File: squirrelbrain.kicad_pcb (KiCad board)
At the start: 2 copper layers, 26.1 x 27.8 mm, 21 parts, among them J1 Conn_01x01, J2 Conn_01x01, J3 Conn_01x03, J4 Conn_01x02, J5 Conn_01x02, Q1 SISS80DN-T1-GE3, U1 SEEEDUINO-XIAO-ESP32S3, U2 THVD1420DRLR, U3 THVD1420DRLR, U5 RPM5.0-6.0, U6 SN74LVC2G125DCUR

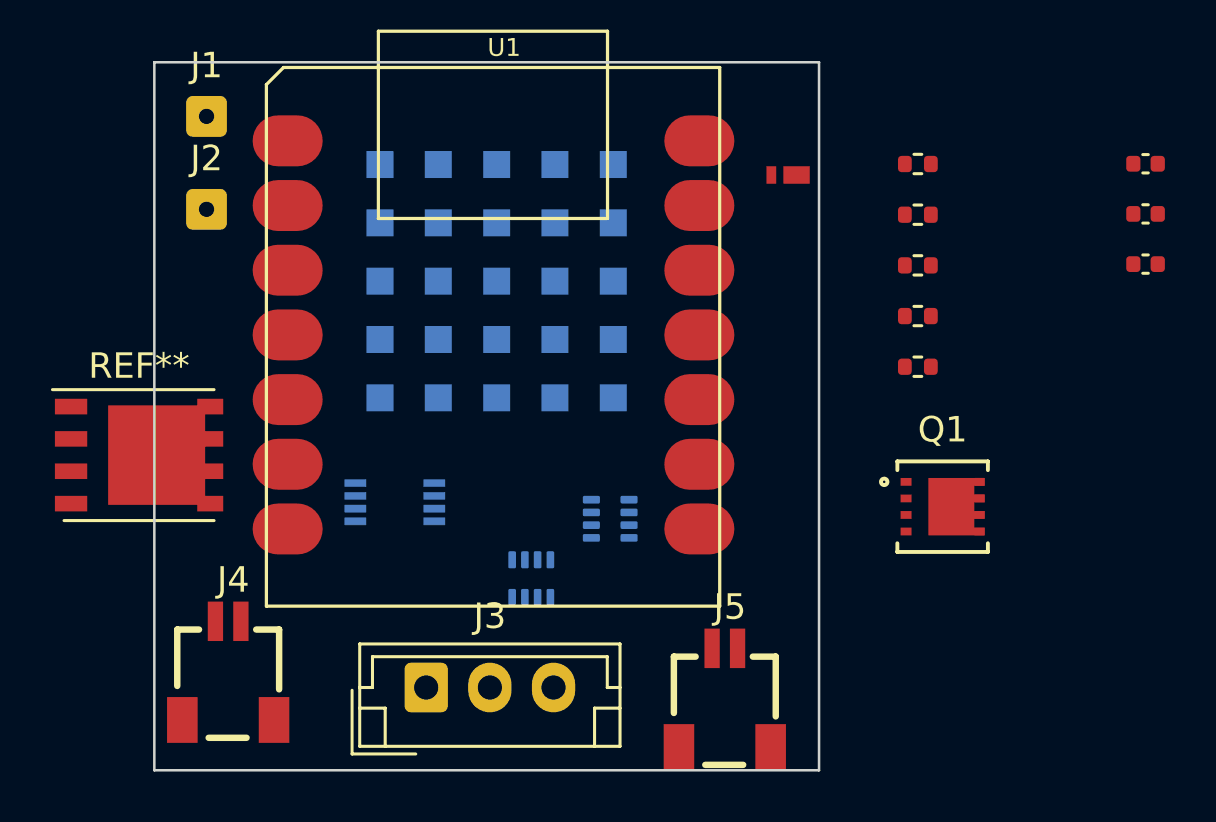
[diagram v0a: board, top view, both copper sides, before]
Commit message: chose high side load switches
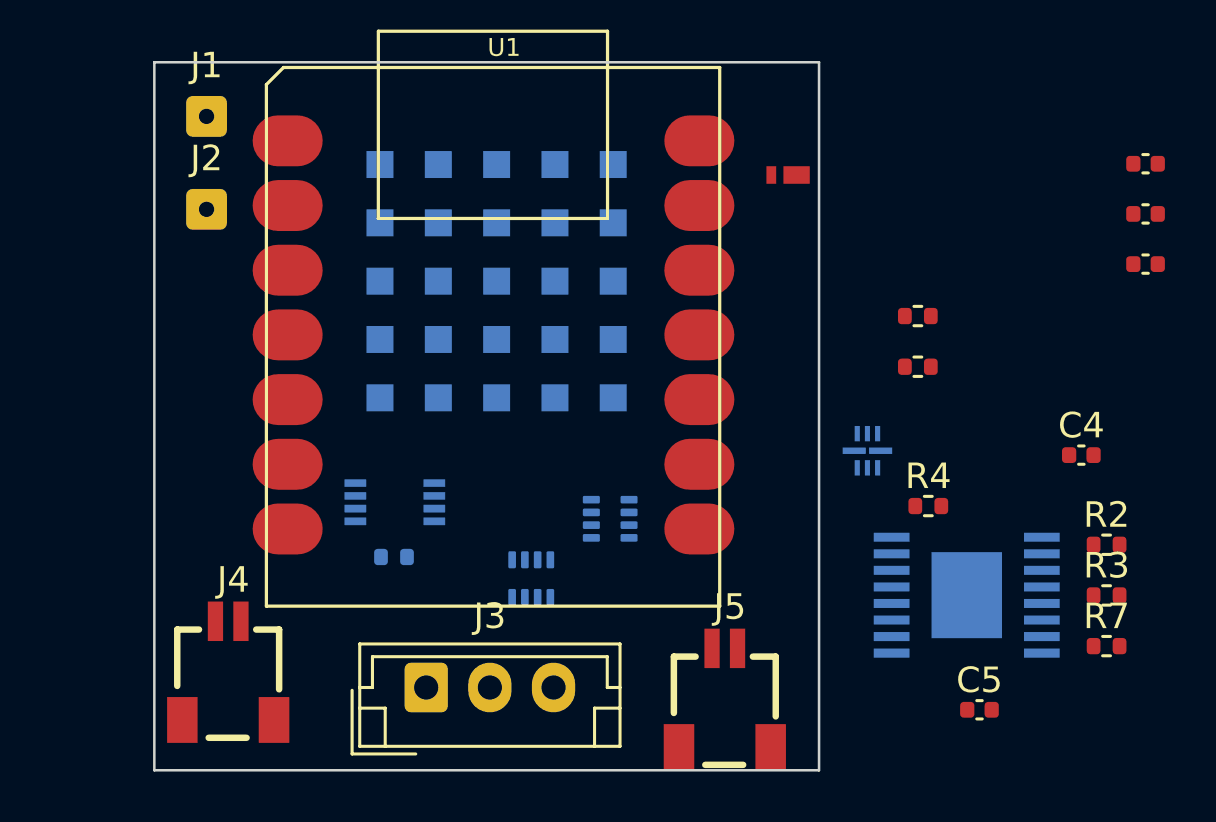
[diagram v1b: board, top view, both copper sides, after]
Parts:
- removed Q1: SISS80DN-T1-GE3, squirrelbrain:SISS80DN
- removed REF**: PowerPAK_SO-8_Single, Package_SO:PowerPAK_SO-8_Single
- added C4: 100nF, Capacitor_SMD:C_0402_1005Metric, F.Cu at (179.5, 98.0)
- added C5: 100nF, Capacitor_SMD:C_0402_1005Metric, F.Cu at (175.5, 108.0)
- added R4: 1k, Resistor_SMD:R_0402_1005Metric, F.Cu at (173.5, 100.0)
- added R7: 10k, Resistor_SMD:R_0402_1005Metric, F.Cu at (180.5, 105.5)
- added U7: TPS1HB08AQPWPRQ1, squirrelbrain:TPS1HB08, B.Cu at (175.0, 103.5)
- added U8: TPS22992SRXNR, squirrelbrain:TPS22992S, B.Cu at (171.1, 97.8)
- R1: moved to B.Cu
- R2: value 54.9k -> 10k
- R3: value 13.7k -> 10k
- moved R1 25.7 mm to (152.5, 102.0), turned to 180 degrees
- moved R3 14.9 mm to (180.5, 103.5)
- moved R2 14.9 mm to (180.5, 101.5)
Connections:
- J3 pad 2: VBUS -> +5VP
- R2 pad 1: /BUS_SENSE -> GND
- R2 pad 2: VBUS -> /MOTOR_ON
- R3 pad 2: /BUS_SENSE -> Net-(U7-SEL1)
- U1 pad 1: unconnected-(U1-PA02_A0_D0-Pad1) -> /MOTOR_ON
- U1 pad 2: /BUS_SENSE -> /GPIO1

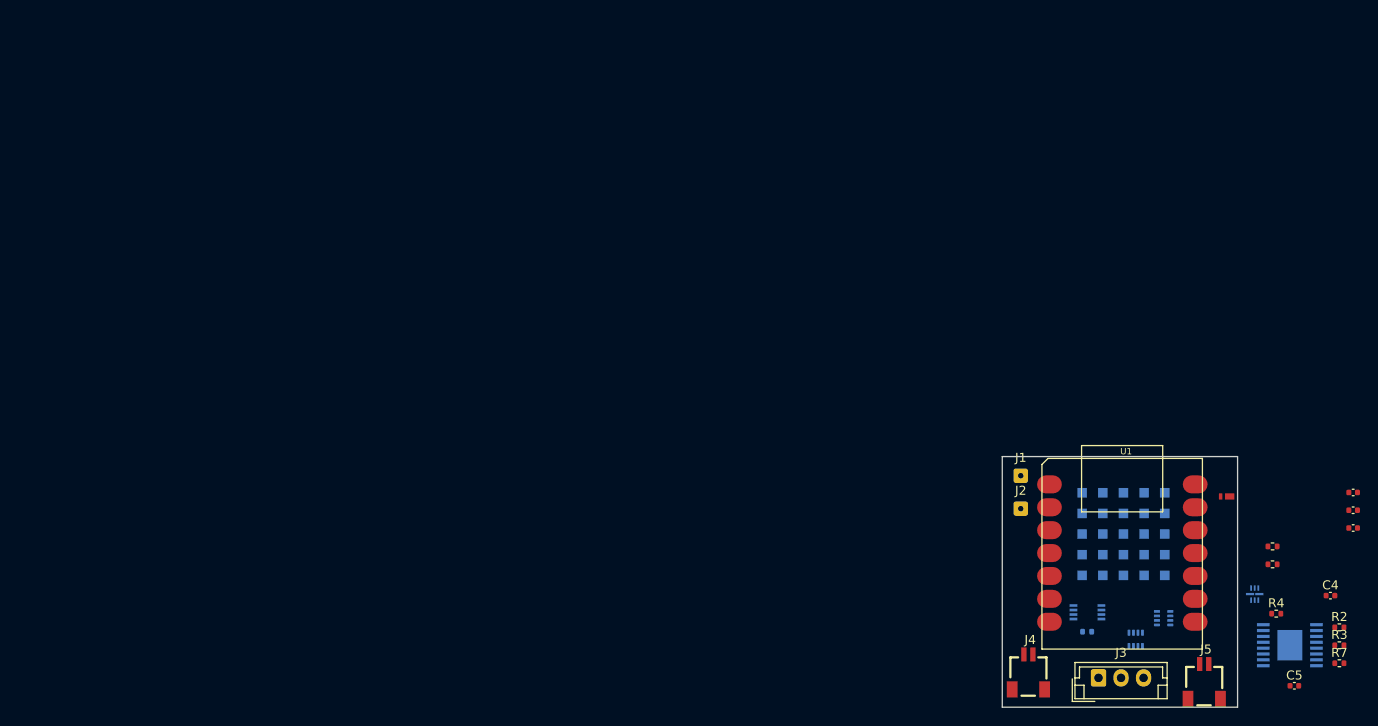
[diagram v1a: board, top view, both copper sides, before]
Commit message: add xt30, start routing
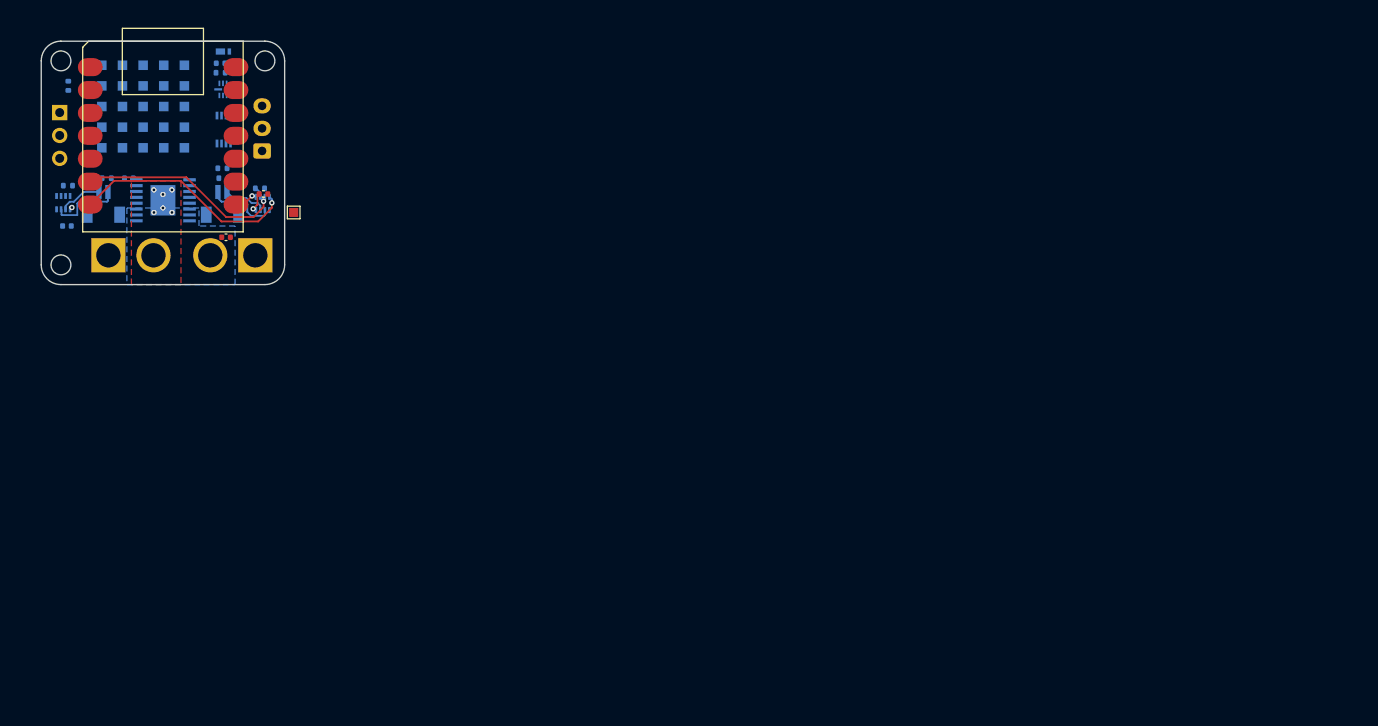
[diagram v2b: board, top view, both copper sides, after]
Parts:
- removed the J2 at (145.2, 88.3)
- added J3: BM02B-SRSS-TB_LF__SN_, squirrelbrain:JST_BM02B-SRSS-TB_LF__SN_, B.Cu at (43.4, 55.8)
- added J6: GPIO1, Connector_PinSocket_2.54mm:PinSocket_1x03_P2.54mm_Vertical, B.Cu at (38.5, 44.4)
- added TP1: SNS, TestPoint:TestPoint_Pad_1.0x1.0mm, F.Cu at (64.5, 55.5)
- C1: renamed from C4; moved to B.Cu
- C3: renamed from C1; moved to B.Cu
- C5: renamed from C2; moved to B.Cu
- D1, R5: moved to B.Cu
- J1: value Conn_01x01 -> BM02B-SRSS-TB_LF__SN_; footprint Connector_Wire:SolderWire-0.1sqmm_1x01_D0.4mm_OD1mm -> squirrelbrain:JST_BM02B-SRSS-TB_LF__SN_; moved to B.Cu
- J2: renamed from J3; moved to B.Cu
- J4: value Conn_01x02 -> BATT; footprint squirrelbrain:JST_SM02B-SRSS-TB(LF)(SN) -> squirrelbrain:AMASS_XT30U-M_1x02_P5.0mm_Vertical; moved to B.Cu
- J5: value Conn_01x02 -> BLDC_PWR; footprint squirrelbrain:JST_SM02B-SRSS-TB(LF)(SN) -> squirrelbrain:AMASS_XT30U-F_1x02_P5.0mm_Vertical; moved to B.Cu
- R1: renamed from R4; moved to B.Cu
- R2: renamed from R3; moved to B.Cu
- R3: renamed from R7; moved to B.Cu
- R4: renamed from R2; moved to B.Cu
- R7: renamed from R6; moved to B.Cu
- U2: renamed from U7; value TPS1HB08AQPWPRQ1 -> TPS1HB08BQPWPRQ1
- moved R4 153.3 mm to (39.5, 41.5), turned to -90 degrees
- moved R2 146.2 mm to (43.8, 51.7), turned to 180 degrees
- moved C5 146.1 mm to (39.3, 57.0)
- moved C1 141.1 mm to (46.2, 51.7), turned to 180 degrees
- moved R7 140.1 mm to (39.5, 52.5), turned to 180 degrees
- moved R3 135.0 mm to (56.7, 51.7), turned to 180 degrees
- moved U2 134.4 mm to (50.0, 54.1)
- moved C3 134.3 mm to (56.4, 39.0), turned to 180 degrees
- moved U7 130.5 mm to (39.0, 54.4), turned to -90 degrees
- moved C2 128.5 mm to (57.0, 58.2)
- moved U3 127.4 mm to (56.7, 41.9)
- moved R1 126.9 mm to (56.6, 50.6), turned to 180 degrees
- moved C4 126.4 mm to (61.1, 53.5)
- moved D1 121.8 mm to (56.7, 37.6), turned to 180 degrees
- moved R5 119.1 mm to (60.8, 52.8), turned to 180 degrees
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- renumbered C5 to C2, C3 to C4, R1 to R6, U5 to U1, U8 to U3, U1 to U4, U2 to U5, U3 to U7
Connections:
- C2 pad 1: VBUS -> Net-(J5-Pin_2)
- J1 pad 1: +BATT -> /RS485_0A
- J4 pad 1: /RS485_0A -> GND
- J4 pad 2: /RS485_0B -> +BATT
- J5 pad 1: /RS485_1A -> GND
- J5 pad 2: /RS485_1B -> Net-(J5-Pin_2)
- U2 pad 10: VBUS -> Net-(J5-Pin_2)
- U2 pad 11: VBUS -> Net-(J5-Pin_2)
- U2 pad 6: VBUS -> Net-(J5-Pin_2)
- U2 pad 7: VBUS -> Net-(J5-Pin_2)
- U2 pad 8: VBUS -> Net-(J5-Pin_2)
- U2 pad 9: VBUS -> Net-(J5-Pin_2)
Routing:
- net /UART0_TX: track 0.00 -> 25.1 mm, vias 0 -> 1
- net /UART0_DE: track 0.00 -> 24.7 mm, vias 0 -> 1
- net /RS485_1B: track 0.00 -> 8.15 mm
- net /RS485_0A: track 0.00 -> 7.76 mm
- net /RS485_0B: track 0.00 -> 4.77 mm
- net /RS485_1A: track 0.00 -> 4.74 mm
- net /UART0_RX: track 0.00 -> 2.58 mm, vias 0 -> 1
- net +3V3: track 0.00 -> 2.29 mm, vias 0 -> 1
- net GND: track 0.00 -> 0.29 mm, vias 0 -> 1
- net +BATT: vias 0 -> 6
- added copper zone on F.Cu, net +BATT
- added copper zone on B.Cu, net Net-(J5-Pin_2)
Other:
- board size 26.1 x 27.8 mm -> 27 x 27 mm

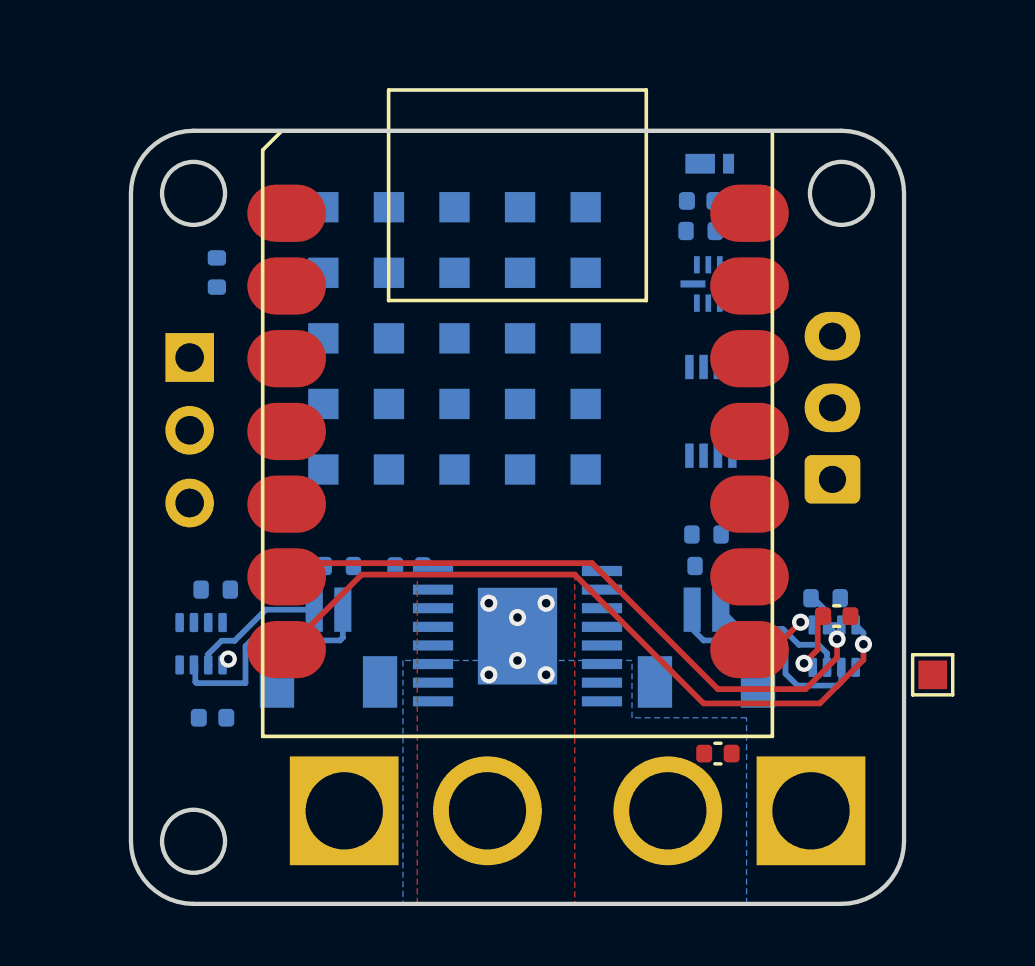
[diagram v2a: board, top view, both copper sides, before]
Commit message: finished routing? need to add 3v3 breakout
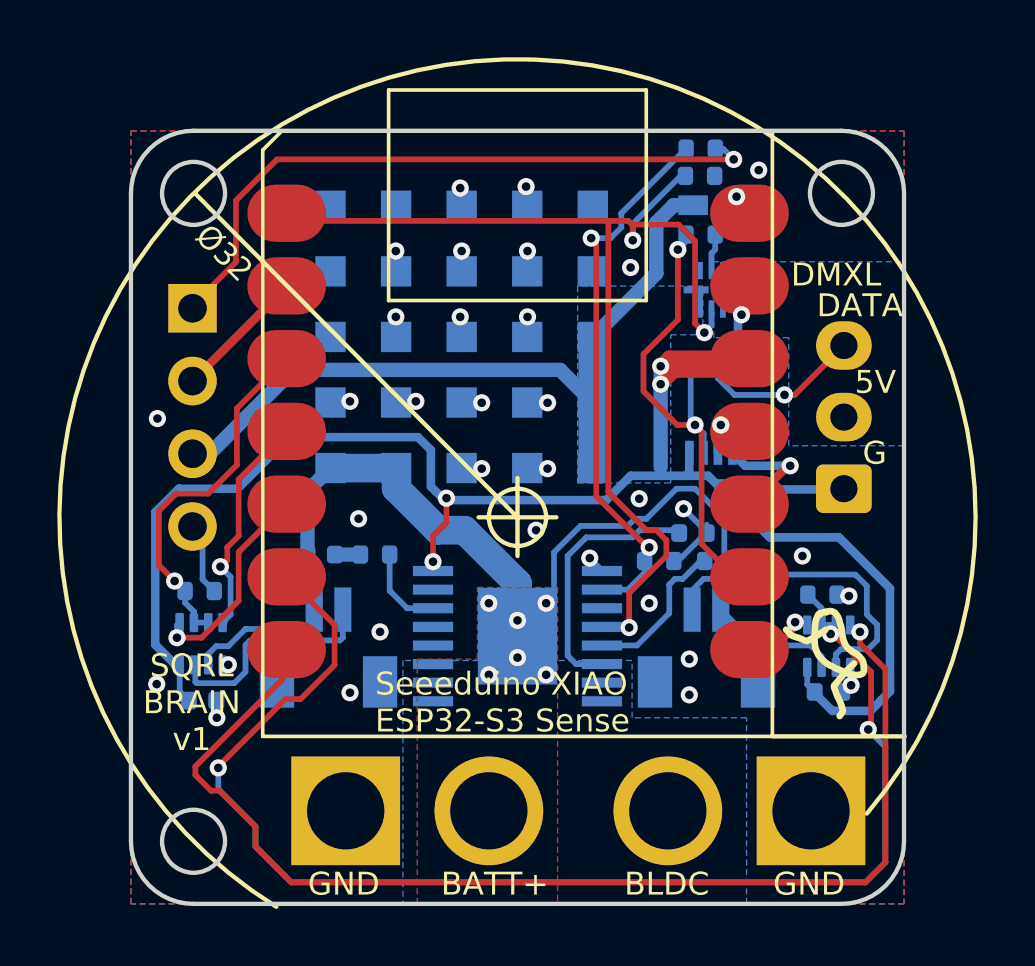
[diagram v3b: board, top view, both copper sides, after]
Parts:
- removed TP1: SNS, TestPoint:TestPoint_Pad_1.0x1.0mm
- added G***: LOGO, LOGO, F.Cu at (60.8, 55.1)
- added R8: 10k, Resistor_SMD:R_0402_1005Metric, B.Cu at (56.4, 37.1)
- C2, C4: moved to B.Cu
- J6: footprint Connector_PinSocket_2.54mm:PinSocket_1x03_P2.54mm_Vertical -> Connector_PinSocket_2.54mm:PinSocket_1x04_P2.54mm_Vertical
- moved R4 17.2 mm to (56.4, 38.1), turned to 180 degrees
- moved C3 10.1 mm to (57.6, 49.0), turned to 0 degrees
- moved C2 7.75 mm to (56.1, 50.5)
- moved C1 3.09 mm to (43.1, 51.3), turned to 0 degrees
- moved C4 2.67 mm to (60.9, 56.1)
- moved R1 1.89 mm to (55.0, 51.5)
- moved J6 1.72 mm to (38.6, 42.7)
- moved D1 1.47 mm to (56.5, 39.1)
- moved R2 1.33 mm to (45.0, 51.3), turned to 0 degrees
- moved C5 0.69 mm to (39.0, 56.4)
- moved R7 0.56 mm to (38.9, 52.6)
- moved J2 0.52 mm to (61.4, 49.0)
- moved R3 0.38 mm to (57.0, 51.5), turned to 0 degrees
- moved U1 0.25 mm to (48.0, 43.7)
- moved U3 0.23 mm to (56.8, 42.1), turned to 0 degrees
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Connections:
- net Net-(U2-SNS) renamed /SNS
- J6 pad 1: /GPIO1 -> Net-(J6-Pin_1)
- J6 pad 2: +5V -> /GPIO1
- J6 pad 3: GND -> +5V
- U2 pad 16: unconnected-(U2-DIA_EN-Pad16) -> +3V3
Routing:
- net +3V3: track 2.29 -> 59.4 mm, vias 1 -> 4
- net /MOTOR_ON: track 0.00 -> 38.3 mm, vias 0 -> 3
- net +5V: track 0.00 -> 27.5 mm
- net +BATT: track 0.00 -> 24.6 mm
- net Net-(J6-Pin_1): track 0.00 -> 23.2 mm, vias 0 -> 1
- net /UART0_DE: track 24.7 -> 46.4 mm, vias 1 -> 3
- net /SNS: track 0.00 -> 19.3 mm, vias 0 -> 2
- net /UART2_DE: track 0.00 -> 18.2 mm, vias 0 -> 2
- net GND: track 0.29 -> 16.8 mm, vias 1 -> 34
- net /UART0_TX: track 25.1 -> 40.5 mm
- net /UART1_DE: track 0.00 -> 12.2 mm, vias 0 -> 1
- net Net-(J5-Pin_2): track 0.00 -> 9.10 mm
- net /UART1_TX: track 0.00 -> 7.97 mm, vias 0 -> 1
- net /UART1_RX: track 0.00 -> 7.32 mm, vias 0 -> 1
- net /DMXL_DATA: track 0.00 -> 6.12 mm, vias 0 -> 1
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- added copper zone on B.Cu, net +5V
- added copper zone on B.Cu, net +5VP
- added copper zone on B.Cu, net GND
- added copper zone on F.Cu, net GND
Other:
- board text added: "0A"
- board text added: "0B"
- board text added: "1A"
- board text added: "1B"
- board text added: "5V"
- board text added: "5V: 6A max"
- board text added: "BATT+"
- board text added: "BLDC"
- board text added: "D1"
- board text added: "DATA"
- board text added: "DMXL"
- board text added: "G"
- board text added: "GND"
- board text added: "JST-EH"
- board text added: "JST-SH RS485"
- board text added: "SNS"
- board text added: "SQRL BRAIN v1"
- board text added: "Seeeduino XIAO ESP32-S3 Sense"
- board text added: "Ø32"

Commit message: rect test pads for 3v3
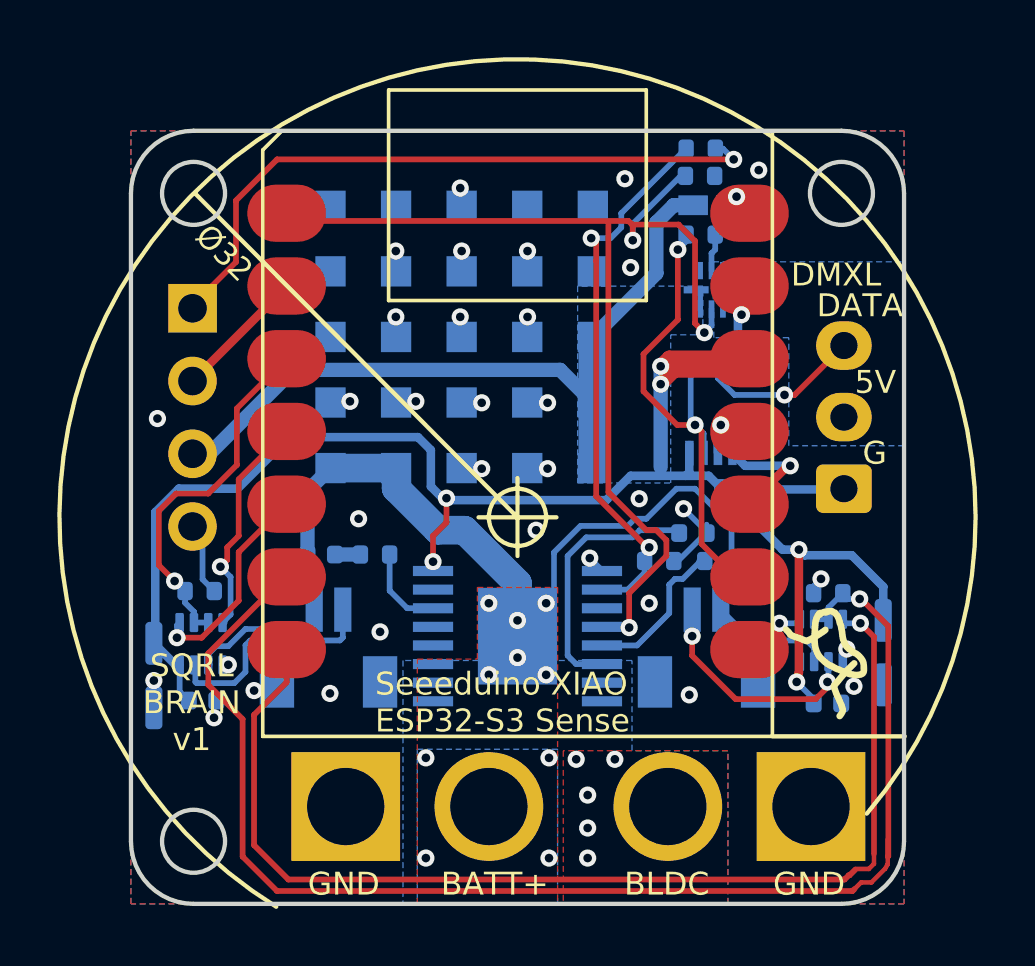
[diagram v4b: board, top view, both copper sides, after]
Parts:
- added TP2: TestPoint, squirrelbrain:TestPoint_Pad_Rect, B.Cu at (62.8, 53.6)
- added TP3: TestPoint, squirrelbrain:TestPoint_Pad_Rect, B.Cu at (62.8, 55.9)
- added TP4: TestPoint, squirrelbrain:TestPoint_Pad_Rect, B.Cu at (37.3, 54.4)
- added TP5: TestPoint, squirrelbrain:TestPoint_Pad_Rect, B.Cu at (37.3, 56.7)
- moved C4 0.40 mm to (60.8, 56.5)
- moved U5 0.33 mm to (60.6, 54.3)
- moved R5 0.21 mm to (60.9, 52.7), turned to 0 degrees
- moved J4 0.15 mm to (44.0, 60.1)
- moved J5 0.15 mm to (60.2, 60.1)
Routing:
- net /RS485_0A: track 11.3 -> 7.84 mm, vias 0 -> 2
- net /UART0_TX: track 40.5 -> 38.9 mm
- net GND: track 16.8 -> 15.6 mm
- net /UART0_DE: track 46.4 -> 47.5 mm, vias 3 -> 1
- net +3V3: track 59.4 -> 59.1 mm, vias 4 -> 6
- net +BATT: vias 6 -> 10
- net Net-(J5-Pin_2): vias 0 -> 5
- added copper zone on B.Cu, net +BATT
- added copper zone on F.Cu, net Net-(J5-Pin_2)
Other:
- board text added: "+"
- board text added: "-"
- board text added: "RS485"
- board text removed: "JST-SH RS485"
